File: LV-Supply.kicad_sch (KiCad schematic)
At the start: 20 parts, among them U11 LMR16006XDDCR

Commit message: Cleaned up the hierarchy
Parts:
- TP65, TP67, TP68: footprint TestPoint:TestPoint_Pad_1.5x1.5mm -> TestPoint:TestPoint_Pad_D1.0mm
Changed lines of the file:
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@@
 			)
 		)
-		(property "Footprint" "TestPoint:TestPoint_Pad_1.5x1.5mm"
+		(property "Footprint" "TestPoint:TestPoint_Pad_D1.0mm"
 			(at 115.57 80.01 0)
 			(hide yes)
@@
 			)
 		)
-		(property "Footprint" "TestPoint:TestPoint_Pad_1.5x1.5mm"
+		(property "Footprint" "TestPoint:TestPoint_Pad_D1.0mm"
 			(at 208.28 80.01 0)
 			(hide yes)
@@
 			)
 		)
-		(property "Footprint" "TestPoint:TestPoint_Pad_1.5x1.5mm"
+		(property "Footprint" "TestPoint:TestPoint_Pad_D1.0mm"
 			(at 124.46 107.95 0)
 			(hide yes)

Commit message: Finished layout
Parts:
- added JP13: SolderJumper_3_Bridged12, Jumper:SolderJumper-3_P1.3mm_Bridged12_RoundedPad1.0x1.5mm_NumberLabels, symbol Jumper:SolderJumper_3_Bridged12
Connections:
- net +VBUS: no longer names the net of C56.1, C57.1, C58.1, R81.1, U11.5 (IN)
- net +VBUS: now also JP13.2 (C)
- new net VBUS: JP13.3 (B)
- new net VPP: JP13.1 (A)
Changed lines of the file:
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@@
+	)
+	(junction
+		(at 39.37 74.93)
+		(diameter 0)
+		(color 0 0 0 0)
 	)
 	(junction
@@
 	)
 	(junction
-		(at 39.37 74.93)
-		(diameter 0)
-		(color 0 0 0 0)
-	)
-	(junction
 		(at 199.39 80.01)
 		(diameter 0)
@@
 	(wire
 		(pts
+			(xy 31.75 67.31) (xy 34.29 67.31)
+		)
+		(stroke
+			(width 0)
+			(type default)
+		)
+	)
+	(wire
+		(pts
 			(xy 100.33 74.93) (xy 124.46 74.93)
 		)
@@
 	(wire
 		(pts
+			(xy 39.37 71.12) (xy 39.37 74.93)
+		)
+		(stroke
+			(width 0)
+			(type default)
+		)
+	)
+	(wire
+		(pts
 			(xy 124.46 102.87) (xy 123.19 102.87)
 		)
@@
 	(wire
 		(pts
+			(xy 46.99 67.31) (xy 44.45 67.31)
+		)
+		(stroke
+			(width 0)
+			(type default)
+		)
+	)
+	(wire
+		(pts
 			(xy 199.39 110.49) (xy 199.39 113.03)
 		)
@@
 	(wire
 		(pts
+			(xy 46.99 66.04) (xy 46.99 67.31)
+		)
+		(stroke
+			(width 0)
+			(type default)
+		)
+	)
+	(wire
+		(pts
 			(xy 154.94 80.01) (xy 177.8 80.01)
 		)
@@
 		(pts
 			(xy 149.86 80.01) (xy 154.94 80.01)
+		)
+		(stroke
+			(width 0)
+			(type default)
+		)
+	)
+	(wire
+		(pts
+			(xy 31.75 66.04) (xy 31.75 67.31)
 		)
 		(stroke
@@
 	)
 	(symbol
+		(lib_id "power:VPP")
+		(at 31.75 66.04 0)
+		(unit 1)
+		(body_style 1)
+		(exclude_from_sim no)
+		(in_bom yes)
+		(on_board yes)
+		(in_pos_files yes)
+		(dnp no)
+		(fields_autoplaced yes)
+		(property "Reference" "#PWR021"
+			(at 31.75 69.85 0)
+			(hide yes)
+			(show_name no)
+			(do_not_autoplace no)
+			(effects
+				(font
+					(size 1.27 1.27)
+				)
+			)
+		)
+		(property "Value" "VPP"
+			(at 31.75 60.96 0)
+			(show_name no)
+			(do_not_autoplace no)
+			(effects
+				(font
+					(size 1.27 1.27)
+				)
+			)
+		)
+		(property "Footprint" ""
+			(at 31.75 66.04 0)
+			(hide yes)
+			(show_name no)
+			(do_not_autoplace no)
+			(effects
+				(font
+					(size 1.27 1.27)
+				)
+			)
+		)
+		(property "Datasheet" ""
+			(at 31.75 66.04 0)
+			(hide yes)
+			(show_name no)
+			(do_not_autoplace no)
+			(effects
+				(font
+					(size 1.27 1.27)
+				)
+			)
+		)
+		(property "Description" "Power symbol creates a global label with name \"VPP\""
+			(at 31.75 66.04 0)
+			(hide yes)
+			(show_name no)
+			(do_not_autoplace no)
+			(effects
+				(font
+					(size 1.27 1.27)
+				)
+			)
+		)
+		(pin "1"
+		)
+		(instances
+			(project "nitride-nano"
+				(path "/aaad0350-e7db-44d5-b7ef-99e6416f6948/7f7c4e65-0f35-4876-a2f6-d81218c9fb3e"
+					(reference "#PWR021")
+					(unit 1)
+				)
+			)
+		)
+	)
+	(symbol
 		(lib_id "power:+3V3")
 		(at 222.25 80.01 0)
@@
 	)
 	(symbol
+		(lib_id "power:VBUS")
+		(at 46.99 66.04 0)
+		(unit 1)
+		(body_style 1)
+		(exclude_from_sim no)
+		(in_bom yes)
+		(on_board yes)
+		(in_pos_files yes)
+		(dnp no)
+		(fields_autoplaced yes)
+		(property "Reference" "#PWR055"
+			(at 46.99 69.85 0)
+			(hide yes)
+			(show_name no)
+			(do_not_autoplace no)
+			(effects
+				(font
+					(size 1.27 1.27)
+				)
+			)
+		)
+		(property "Value" "VBUS"
+			(at 46.99 60.96 0)
+			(show_name no)
+			(do_not_autoplace no)
+			(effects
+				(font
+					(size 1.27 1.27)
+				)
+			)
+		)
+		(property "Footprint" ""
+			(at 46.99 66.04 0)
+			(hide yes)
+			(show_name no)
+			(do_not_autoplace no)
+			(effects
+				(font
+					(size 1.27 1.27)
+				)
+			)
+		)
+		(property "Datasheet" ""
+			(at 46.99 66.04 0)
+			(hide yes)
+			(show_name no)
+			(do_not_autoplace no)
+			(effects
+				(font
+					(size 1.27 1.27)
+				)
+			)
+		)
+		(property "Description" "Power symbol creates a global label with name \"VBUS\""
+			(at 46.99 66.04 0)
+			(hide yes)
+			(show_name no)
+			(do_not_autoplace no)
+			(effects
+				(font
+					(size 1.27 1.27)
+				)
+			)
+		)
+		(pin "1"
+		)
+		(instances
+			(project "nitride-nano"
+				(path "/aaad0350-e7db-44d5-b7ef-99e6416f6948/7f7c4e65-0f35-4876-a2f6-d81218c9fb3e"
+					(reference "#PWR055")
+					(unit 1)
+				)
+			)
+		)
+	)
+	(symbol
 		(lib_id "power:GND")
 		(at 199.39 113.03 0)
@@
 	)
 	(symbol
-		(lib_id "power:VBUS")
-		(at 39.37 74.93 0)
-		(unit 1)
-		(body_style 1)
-		(exclude_from_sim no)
-		(in_bom yes)
-		(on_board yes)
-		(in_pos_files yes)
-		(dnp no)
-		(property "Reference" "#PWR0156"
-			(at 39.37 74.93 0)
-			(hide yes)
-			(show_name no)
-			(do_not_autoplace no)
-			(effects
-				(font
-					(size 1.27 1.27)
-				)
-			)
-		)
-		(property "Value" "+VBUS"
-			(at 41.91 69.85 0)
-			(show_name no)
-			(do_not_autoplace no)
-			(effects
-				(font
-					(size 1.27 1.27)
-				)
-				(justify right)
-			)
-		)
-		(property "Footprint" ""
-			(at 39.37 74.93 0)
-			(show_name no)
-			(do_not_autoplace no)
-			(effects
-				(font
-					(size 1.27 1.27)
-				)
-			)
-		)
-		(property "Datasheet" ""
-			(at 39.37 74.93 0)
-			(show_name no)
-			(do_not_autoplace no)
-			(effects
-				(font
-					(size 1.27 1.27)
-				)
-			)
-		)
-		(property "Description" ""
-			(at 39.37 74.93 0)
-			(show_name no)
-			(do_not_autoplace no)
-			(effects
-				(font
-					(size 1.27 1.27)
-				)
-			)
-		)
-		(pin "1"
-		)
-		(instances
-			(project "nitride-nano"
-				(path "/aaad0350-e7db-44d5-b7ef-99e6416f6948/7f7c4e65-0f35-4876-a2f6-d81218c9fb3e"
-					(reference "#PWR0156")
-					(unit 1)
-				)
-			)
-		)
-	)
-	(symbol
 		(lib_id "0_passives:C_0805")
 		(at 39.37 80.01 0)
@@
 					(unit 1)
 				)
+			)
+		)
+	)
+	(symbol
+		(lib_id "Jumper:SolderJumper_3_Bridged12")
+		(at 39.37 67.31 0)
+		(unit 1)
+		(body_style 1)
+		(exclude_from_sim no)
+		(in_bom no)
+		(on_board yes)
+		(in_pos_files yes)
+		(dnp no)
+		(property "Reference" "JP13"
+			(at 39.37 63.5 0)
+			(show_name no)
+			(do_not_autoplace no)
+			(effects
+				(font
+					(size 1.27 1.27)
+				)
+			)
+		)
+		(property "Value" "SolderJumper_3_Bridged12"
+			(at 39.37 60.96 0)
+			(hide yes)
+			(show_name no)
+			(do_not_autoplace no)
+			(effects
+				(font
+					(size 1.27 1.27)
+				)
+			)
+		)
+		(property "Footprint" "Jumper:SolderJumper-3_P1.3mm_Bridged12_RoundedPad1.0x1.5mm_NumberLabels"
+			(at 39.37 67.31 0)
+			(hide yes)
+			(show_name no)
+			(do_not_autoplace no)
+			(effects
+				(font
+					(size 1.27 1.27)
+				)
+			)
+		)
+		(property "Datasheet" ""
+			(at 39.37 82.55 0)
+			(hide yes)
+			(show_name no)
+			(do_not_autoplace no)
+			(effects
+				(font
+					(size 1.27 1.27)
+				)
+			)
+		)
+		(property "Description" "3-pole Solder Jumper, pins 1+2 closed/bridged"
+			(at 39.37 80.01 0)
+			(hide yes)
+			(show_name no)
+			(do_not_autoplace no)
+			(effects
+				(font
+					(size 1.27 1.27)
+				)
+			)
+		)
+		(pin "3"
+		)
+		(pin "1"
+		)
+		(pin "2"
+		)
+		(instances
+			(project "nitride-nano"
+				(path "/aaad0350-e7db-44d5-b7ef-99e6416f6948/7f7c4e65-0f35-4876-a2f6-d81218c9fb3e"
+					(reference "JP13")
+					(unit 1)
+				)

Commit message: Started routing
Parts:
- added D22: LED, LED_SMD:LED_0603_1608Metric, symbol Device:LED
- added R77: 1k, Resistor_SMD:R_0402_1005Metric, symbol Device:R
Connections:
- net +3V3: now also D22.2 (A)
- net GND: now also R77.1
- new net: D22.1 (K), R77.2
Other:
- note added: "65V max is wel beetje te dicht in de buurt van 60Vin maybe"
- title: (none) -> Nitride-Nano
- moved on the sheet: C55, C56, C57, C58, C59, C60, C61, C62, D14, JP12, JP13, L2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

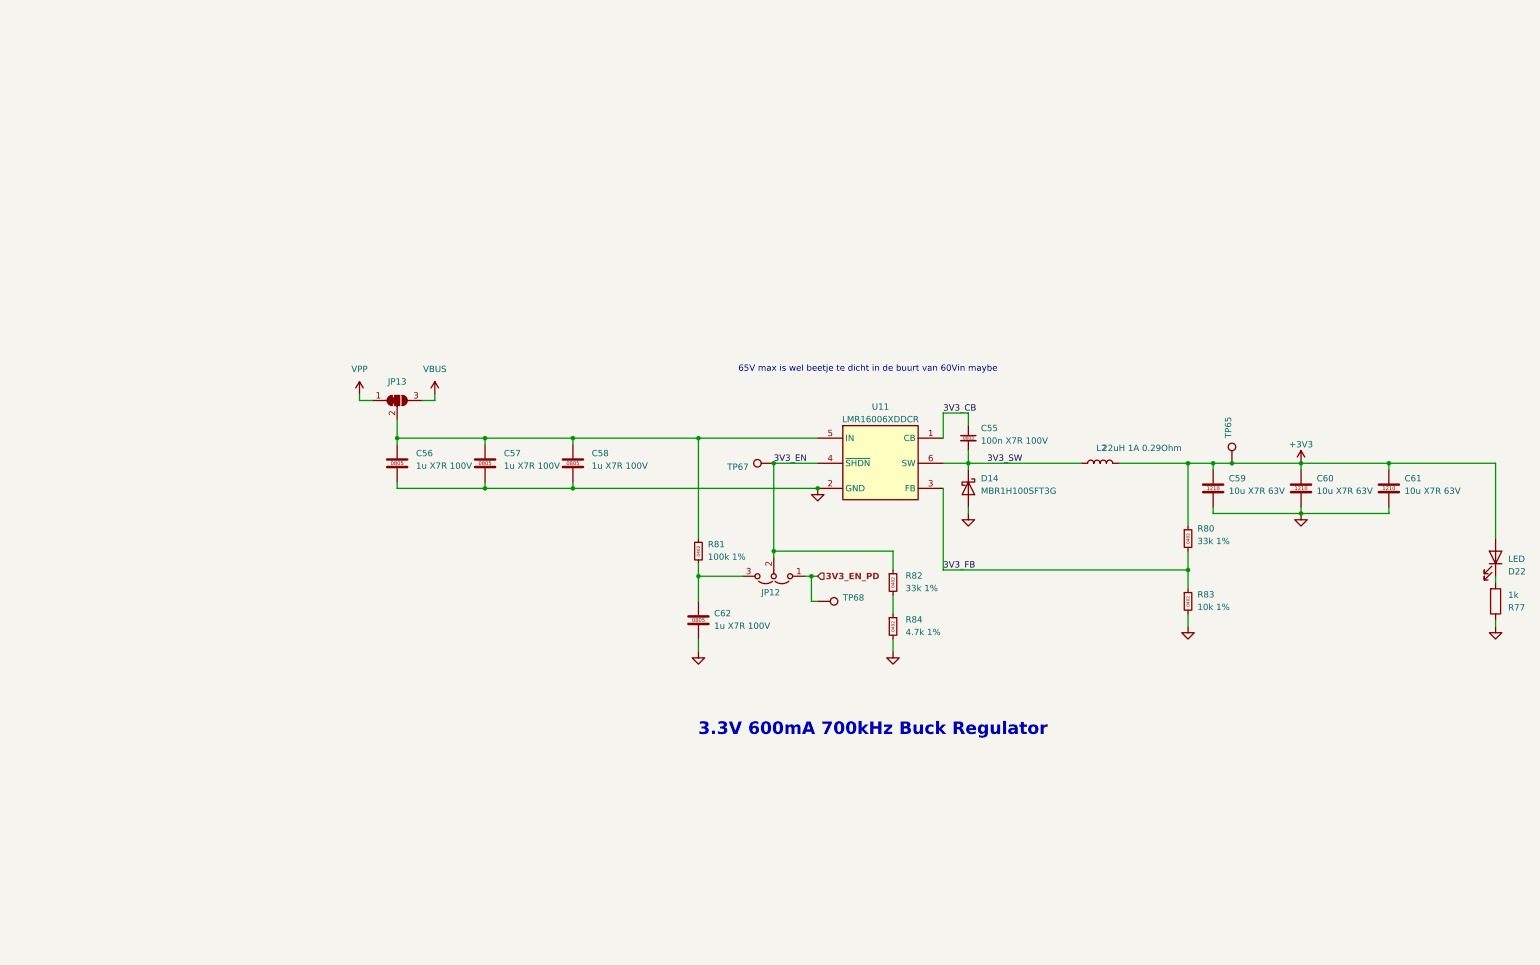
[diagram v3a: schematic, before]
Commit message: Added 5V fan psu
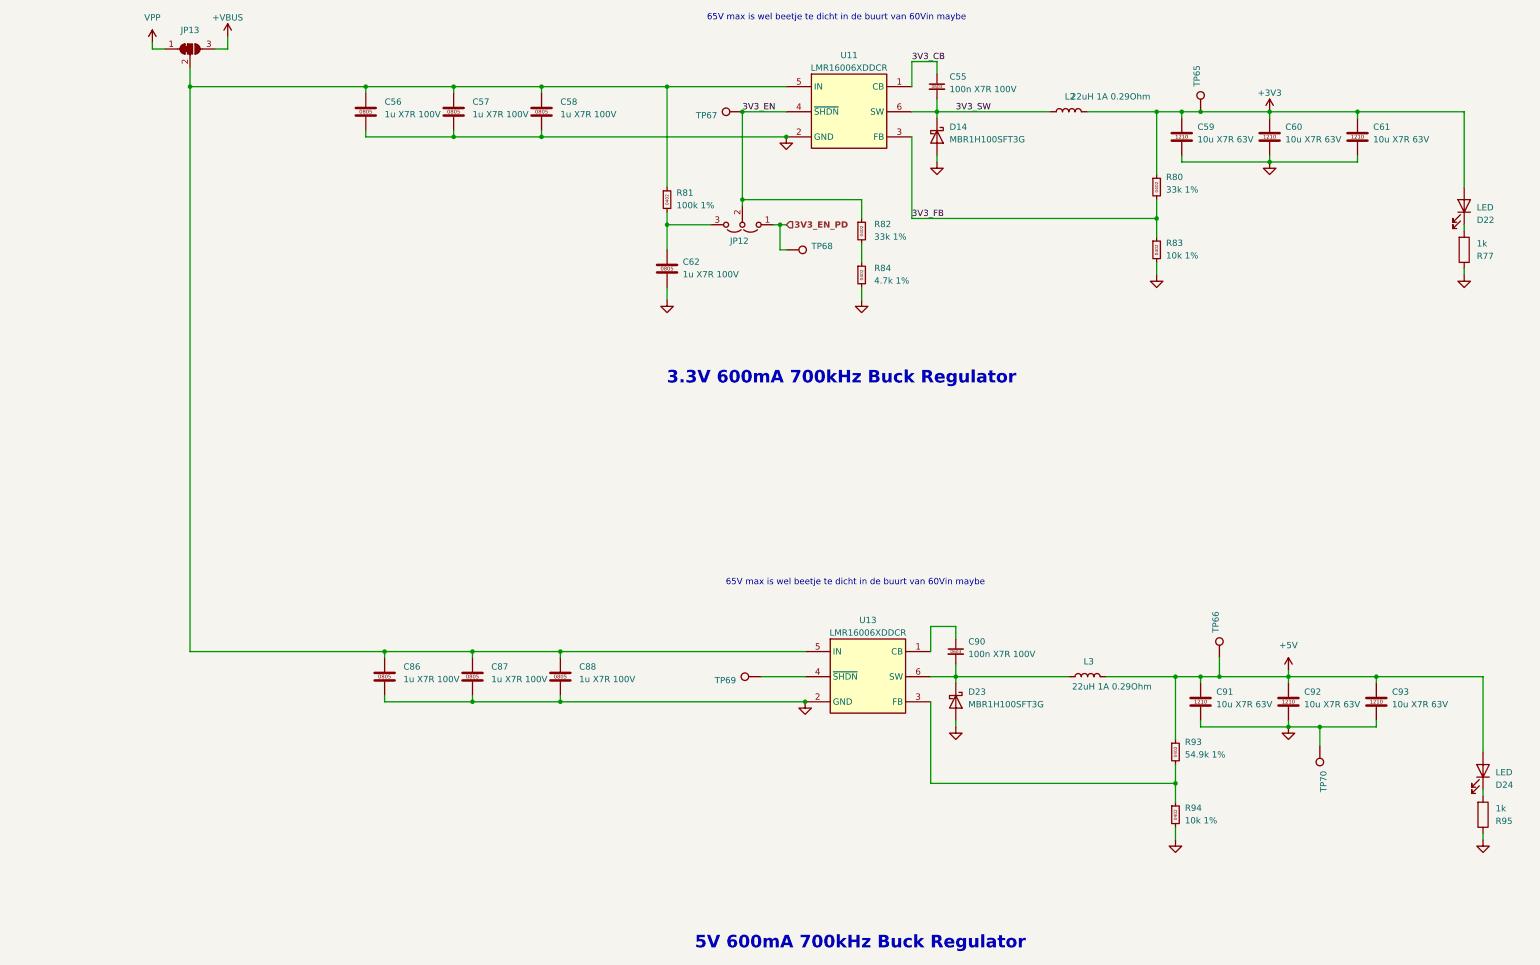
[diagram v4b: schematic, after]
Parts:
- added C86, C87, C88: 1u X7R 100V, Capacitor_SMD:C_0805_2012Metric, symbol 0_passives:C_0805
- added C90: 100n X7R 100V, Capacitor_SMD:C_0603_1608Metric, symbol 0_passives:C_0603
- added C91, C92, C93: 10u X7R 63V, Capacitor_SMD:C_1210_3225Metric, symbol 0_passives:C_1210
- added D23: MBR1H100SFT3G, Altium_port:sod-123fl_305p_260x160x90_n, symbol Device:D_Schottky
- added D24: LED, LED_SMD:LED_0603_1608Metric, symbol Device:LED
- added L3: 22uH 1A 0.29Ohm, Altium_port:SWPA4030S220MT, symbol Device:L
- added R93: 54.9k 1%, Resistor_SMD:R_0402_1005Metric, symbol 0_passives:R_0402
- added R94: 10k 1%, Resistor_SMD:R_0402_1005Metric, symbol 0_passives:R_0402
- added R95: 1k, Resistor_SMD:R_0402_1005Metric, symbol Device:R
- added TP66, TP69, TP70: tp_round_70, TestPoint:TestPoint_Pad_D1.0mm, symbol Connector:TestPoint
- added U13: LMR16006XDDCR, Altium_port:sot6_p95_290x180x110_n, symbol 0_PD240W:LMR16006XDDCR
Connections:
- net GND: now also C86.2, C87.2, C88.2, C91.2, C92.2, C93.2, D23.2 (A), R94.2, R95.1, TP70.1, U13.2 (GND)
- net at C56.1, C57.1, C58.1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: now also C86.1, C87.1, C88.1, U13.5 (IN)
- net VBUS renamed +VBUS
- new net: C90.2, D23.1 (K), L3.1, U13.6 (SW)
- new net: C90.1, U13.1 (CB)
- new net: R93.2, R94.1, U13.3 (FB)
- new net: TP69.1, U13.4 (~{SHDN})
- new net: D24.1 (K), R95.2
- new net +5V: C91.1, C92.1, C93.1, D24.2 (A), L3.2, R93.1, TP66.1
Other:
- note added: "5V 600mA 700kHz Buck Regulator"
- moved on the sheet: C55, C56, C57, C58, C59, C60, C61, C62, D14, D22, JP12, JP13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
